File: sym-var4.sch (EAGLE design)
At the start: 23 parts, among them SW1 SPST_TACT-KMR2, U1 L9110, U2 L9110, U3 ESP8266MODULES_ESP12E, U4 AP2112K-3.3V, U5 ALC5628

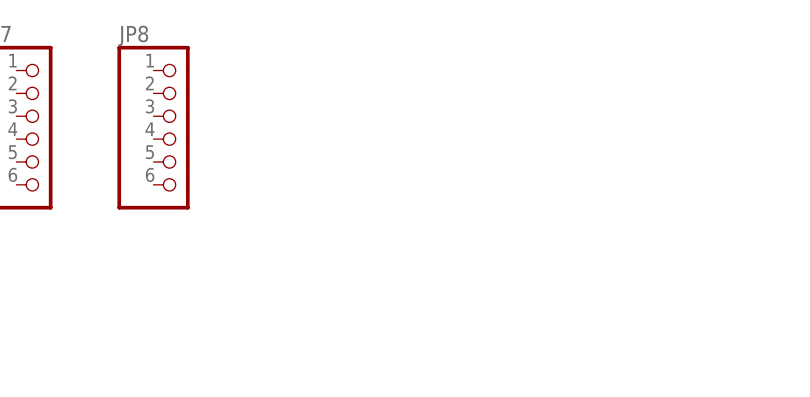
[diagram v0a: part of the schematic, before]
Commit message: Added Prog Connector
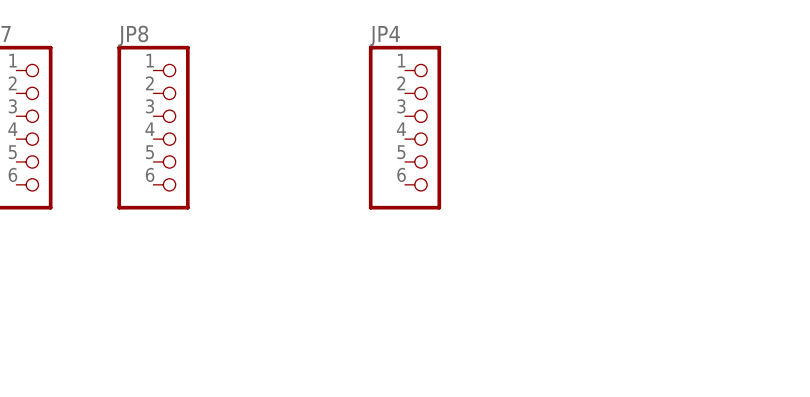
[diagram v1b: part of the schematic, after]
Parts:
- added JP4: (no value), adafruit:PINHD-1X6
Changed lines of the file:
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@@
 <part name="GND18" library="supply1" deviceset="GND" device=""/>
 <part name="+3V8" library="supply1" deviceset="+3V3" device=""/>
+<part name="JP4" library="adafruit" deviceset="PINHD-1X6" device=""/>
 </parts>
 <sheets>
@@
 <instance part="GND18" gate="1" x="314.96" y="208.28"/>
 <instance part="+3V8" gate="G$1" x="294.64" y="154.94"/>
+<instance part="JP4" gate="A" x="238.76" y="220.98"/>
 </instances>
 <busses>

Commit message: Layout complete
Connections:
- new net N$9: JP8.1, JP8.2, JP8.3, JP8.4, JP8.5, JP8.6
- net +3V3: now also JP7.6
- net ESP_RXD: now also JP4.3
- net ESP_TXD: now also JP4.2
- net GND: now also JP4.6, JP7.1, JP7.2, JP7.3, JP7.4, JP7.5
- net GPIO0: now also JP4.1
- net VBAT: now also JP6.6
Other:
- moved on the sheet: JP4, JP7
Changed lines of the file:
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@@
 <part name="+3V8" library="supply1" deviceset="+3V3" device=""/>
 <part name="JP4" library="adafruit" deviceset="PINHD-1X6" device=""/>
+<part name="+3V9" library="supply1" deviceset="+3V3" device=""/>
+<part name="GND16" library="SparkFun-Aesthetics" deviceset="GND" device=""/>
+<part name="GND19" library="SparkFun-Aesthetics" deviceset="GND" device=""/>
 </parts>
 <sheets>
@@
 <instance part="+3V7" gate="G$1" x="60.96" y="111.76" rot="R90"/>
 <instance part="JP6" gate="A" x="180.34" y="220.98"/>
-<instance part="JP7" gate="A" x="195.58" y="220.98"/>
+<instance part="JP7" gate="A" x="198.12" y="220.98"/>
 <instance part="JP8" gate="A" x="210.82" y="220.98"/>
 <instance part="U3" gate="G$1" x="33.02" y="134.62"/>
@@
 <instance part="GND18" gate="1" x="314.96" y="208.28"/>
 <instance part="+3V8" gate="G$1" x="294.64" y="154.94"/>
-<instance part="JP4" gate="A" x="238.76" y="220.98"/>
+<instance part="JP4" gate="A" x="294.64" y="91.44"/>
+<instance part="+3V9" gate="G$1" x="190.5" y="215.9" rot="R90"/>
+<instance part="GND16" gate="1" x="187.96" y="218.44" rot="R270"/>
+<instance part="GND19" gate="1" x="276.86" y="86.36" rot="R270"/>
 </instances>
 <busses>
@@
 <pinref part="GND17" gate="1" pin="GND"/>
 <pinref part="C7" gate="G$1" pin="2"/>
+</segment>
+<segment>
+<pinref part="JP7" gate="A" pin="5"/>
+<pinref part="JP7" gate="A" pin="4"/>
+<wire x1="195.58" y1="218.44" x2="195.58" y2="220.98" width="0.1524" layer="91"/>
+<pinref part="JP7" gate="A" pin="3"/>
+<wire x1="195.58" y1="220.98" x2="195.58" y2="223.52" width="0.1524" layer="91"/>
+<junction x="195.58" y="220.98"/>
+<pinref part="JP7" gate="A" pin="2"/>
+<wire x1="195.58" y1="223.52" x2="195.58" y2="226.06" width="0.1524" layer="91"/>
+<junction x="195.58" y="223.52"/>
+<pinref part="JP7" gate="A" pin="1"/>
+<wire x1="195.58" y1="226.06" x2="195.58" y2="228.6" width="0.1524" layer="91"/>
+<junction x="195.58" y="226.06"/>
+<wire x1="195.58" y1="218.44" x2="190.5" y2="218.44" width="0.1524" layer="91"/>
+<junction x="195.58" y="218.44"/>
+<pinref part="GND16" gate="1" pin="GND"/>
+</segment>
+<segment>
+<pinref part="JP4" gate="A" pin="6"/>
+<wire x1="279.4" y1="86.36" x2="292.1" y2="86.36" width="0.1524" layer="91"/>
+<pinref part="GND19" gate="1" pin="GND"/>
 </segment>
 </net>
@@
 <junction x="294.64" y="152.4"/>
 </segment>
+<segment>
+<pinref part="JP7" gate="A" pin="6"/>
+<pinref part="+3V9" gate="G$1" pin="+3V3"/>
+<wire x1="195.58" y1="215.9" x2="193.04" y2="215.9" width="0.1524" layer="91"/>
+</segment>
 </net>
 <net name="ESP_RXD" class="0">
@@
 <label x="299.72" y="190.5" size="1.27" layer="95" rot="R180" xref="yes"/>
 </segment>
+<segment>
+<pinref part="JP4" gate="A" pin="3"/>
+<wire x1="292.1" y1="93.98" x2="284.48" y2="93.98" width="0.1524" layer="91"/>
+<label x="284.48" y="93.98" size="1.27" layer="95" rot="R180" xref="yes"/>
+</segment>
 </net>
 <net name="ESP_TXD" class="0">
@@
 <wire x1="317.5" y1="195.58" x2="299.72" y2="195.58" width="0.1524" layer="91"/>
 <label x="299.72" y="195.58" size="1.27" layer="95" rot="R180" xref="yes"/>
+</segment>
+<segment>
+<pinref part="JP4" gate="A" pin="2"/>
+<wire x1="292.1" y1="96.52" x2="284.48" y2="96.52" width="0.1524" layer="91"/>
+<label x="284.48" y="96.52" size="1.27" layer="95" rot="R180" xref="yes"/>
 </segment>
 </net>
@@
 <junction x="121.92" y="190.5"/>
 </segment>
+<segment>
+<pinref part="JP6" gate="A" pin="6"/>
+<wire x1="177.8" y1="215.9" x2="165.1" y2="215.9" width="0.1524" layer="91"/>
+<label x="165.1" y="215.9" size="1.27" layer="95" rot="R180" xref="yes"/>
+</segment>
 </net>
 <net name="1A" class="0">
@@
 <wire x1="317.5" y1="180.34" x2="299.72" y2="180.34" width="0.1524" layer="91"/>
 <label x="299.72" y="180.34" size="1.27" layer="95" rot="R180" xref="yes"/>
+</segment>
+<segment>
+<pinref part="JP4" gate="A" pin="1"/>
+<wire x1="292.1" y1="99.06" x2="284.48" y2="99.06" width="0.1524" layer="91"/>
+<label x="284.48" y="99.06" size="1.27" layer="95" rot="R180" xref="yes"/>
 </segment>
 </net>
@@
 </segment>
 </net>
+<net name="N$9" class="0">
+<segment>
+<pinref part="JP8" gate="A" pin="1"/>
+<pinref part="JP8" gate="A" pin="6"/>
+<wire x1="208.28" y1="228.6" x2="208.28" y2="226.06" width="0.1524" layer="91"/>
+<pinref part="JP8" gate="A" pin="2"/>
+<wire x1="208.28" y1="226.06" x2="208.28" y2="223.52" width="0.1524" layer="91"/>
+<junction x="208.28" y="226.06"/>
+<pinref part="JP8" gate="A" pin="3"/>
+<wire x1="208.28" y1="223.52" x2="208.28" y2="220.98" width="0.1524" layer="91"/>
+<junction x="208.28" y="223.52"/>
+<pinref part="JP8" gate="A" pin="4"/>
+<wire x1="208.28" y1="220.98" x2="208.28" y2="218.44" width="0.1524" layer="91"/>
+<junction x="208.28" y="220.98"/>
+<pinref part="JP8" gate="A" pin="5"/>
+<wire x1="208.28" y1="218.44" x2="208.28" y2="215.9" width="0.1524" layer="91"/>
+<junction x="208.28" y="218.44"/>
+</segment>
+</net>
